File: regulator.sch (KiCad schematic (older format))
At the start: 28 parts, among them IC1 PIC12F675-I/P, Q1 PN2222A, Q2 2N2907A, Q3 BUK9511-55A (Logic Level), Q4 PN2222A, Q5 BUK9511-55A (Logic Level), U1 LM7805

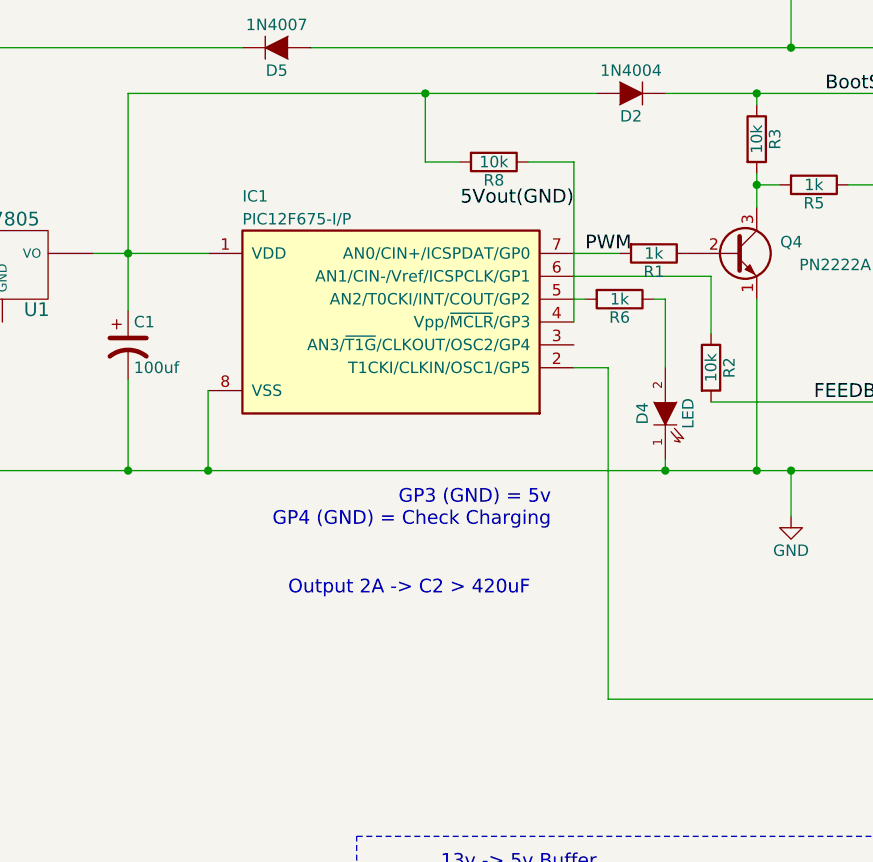
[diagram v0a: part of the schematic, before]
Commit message: Change schematic. It's not compatible with previous. Use VREF for ADC. It help under 5V output setting. ADC pin and LED pin is changed.
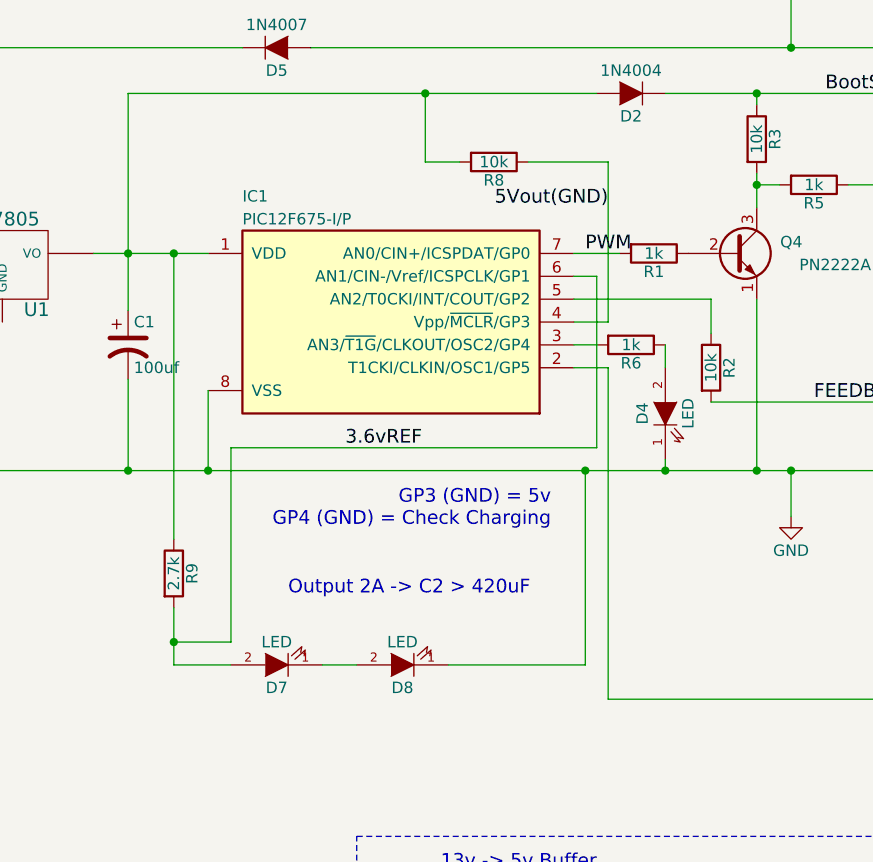
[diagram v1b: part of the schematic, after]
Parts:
- added D7, D8: LED, symbol LED
- added R9: 2.7k, symbol R
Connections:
- net GND: now also D8.1 (K)
- net at C1.1, D2.2 (A), IC1.1 (VDD)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: now also R9.1
- net at IC1.3 (AN3/~T1G~/CLKOUT/OSC2/GP4): now also R6.2
- net at IC1.5 (AN2/T0CKI/INT/COUT/GP2): now also R2.1; no longer R6.2
- net 3.6vREF: now reaches IC1.6 (AN1/CIN-/Vref/ICSPCLK/GP1)
- net 3.6vREF: now also D7.2 (A), R9.2; no longer R2.1
- new net: D7.1 (K), D8.2 (A)
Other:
- moved on the sheet: R6
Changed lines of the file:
@@
 Sheet 1 1
 Title "PWM Regulator v3"
-Date "2015-08-03"
-Rev "1.2k"
+Date "2015-08-05"
+Rev "1.3"
 Comp ""
 Comment1 ""
@@
 L R R6
 U 1 1 55680C08
-P 4050 2950
-F 0 "R6" V 4130 2950 50  0000 C CNN
-F 1 "1k" V 4050 2950 50  0000 C CNN
-F 2 "" V 3980 2950 30  0000 C CNN
-F 3 "" H 4050 2950 30  0000 C CNN
-	1    4050 2950
+P 4100 3150
+F 0 "R6" V 4180 3150 50  0000 C CNN
+F 1 "1k" V 4100 3150 50  0000 C CNN
+F 2 "" V 4030 3150 30  0000 C CNN
+F 3 "" H 4100 3150 30  0000 C CNN
+	1    4100 3150
 	0    1    1    0
 $EndComp
@@
 	0    1    1    0
 $EndComp
-Text Label 3850 2550 2    60   ~ 0
+Text Label 4000 2550 2    60   ~ 0
 5Vout(GND)
 Text Notes 3750 3950 2    60   ~ 0
@@
 Text GLabel 5050 5650 2    60   Output ~ 0
 Vto5v(+)
+Text Notes 3950 5450 2    60   ~ 0
+13v -> 5v Buffer
+$Comp
+L LED D7
+U 1 1 55C1B6BA
+P 2550 4550
+F 0 "D7" H 2550 4650 50  0000 C CNN
+F 1 "LED" H 2550 4450 50  0000 C CNN
+F 2 "" H 2550 4550 60  0000 C CNN
+F 3 "" H 2550 4550 60  0000 C CNN
+	1    2550 4550
+	-1   0    0    1
+$EndComp
+$Comp
+L LED D8
+U 1 1 55C1B8A3
+P 3100 4550
+F 0 "D8" H 3100 4650 50  0000 C CNN
+F 1 "LED" H 3100 4450 50  0000 C CNN
+F 2 "" H 3100 4550 60  0000 C CNN
+F 3 "" H 3100 4550 60  0000 C CNN
+	1    3100 4550
+	-1   0    0    1
+$EndComp
+$Comp
+L R R9
+U 1 1 55C1B943
+P 2100 4150
+F 0 "R9" V 2180 4150 50  0000 C CNN
+F 1 "2.7k" V 2100 4150 50  0000 C CNN
+F 2 "" V 2030 4150 30  0000 C CNN
+F 3 "" H 2100 4150 30  0000 C CNN
+	1    2100 4150
+	1    0    0    -1
+$EndComp
 Wire Wire Line
 	4800 3700 4800 3900
@@
 	5200 2450 5200 3000
 Wire Wire Line
-	3850 2850 4450 2850
-Wire Wire Line
-	4450 2850 4450 3100
-Wire Wire Line
 	4650 2400 4650 2550
 Wire Wire Line
@@
 	4800 1500 4800 1850
 Wire Wire Line
-	3900 2950 3850 2950
-Wire Wire Line
-	4200 2950 4250 2950
-Wire Wire Line
-	4250 2950 4250 3250
-Wire Wire Line
 	4250 3650 4250 3700
 Connection ~ 4250 3700
@@
 	1350 1500 4800 1500
 Wire Wire Line
-	3650 2350 3850 2350
-Wire Wire Line
-	3850 2350 3850 3050
+	3650 2350 4000 2350
 Wire Wire Line
 	3350 2350 3200 2350
@@
 	4650 5850 4650 5650
 Connection ~ 4650 5650
-Text Notes 3950 5450 2    60   ~ 0
-13v -> 5v Buffer
 Wire Notes Line
 	2900 5300 5600 5300
@@
 Wire Notes Line
 	2900 6750 2900 5300
+Wire Wire Line
+	3850 3050 4000 3050
+Wire Wire Line
+	4000 3050 4000 2350
+Wire Wire Line
+	4250 3250 4250 3150
+Wire Wire Line
+	3950 3150 3850 3150
+Wire Wire Line
+	4450 3100 4450 2950
+Wire Wire Line
+	4450 2950 3850 2950
+Wire Wire Line
+	2100 4300 2100 4550
+Wire Wire Line
+	2100 4550 2350 4550
+Wire Wire Line
+	3300 4550 3900 4550
+Wire Wire Line
+	3900 4550 3900 3700
+Connection ~ 3900 3700
+Wire Wire Line
+	2100 4000 2100 2750
+Connection ~ 2100 2750
+Wire Wire Line
+	2750 4550 2900 4550
+Wire Wire Line
+	3850 2850 3950 2850
+Wire Wire Line
+	3950 2850 3950 3600
+Wire Wire Line
+	3950 3600 2350 3600
+Wire Wire Line
+	2350 3600 2350 4450
+Wire Wire Line
+	2350 4450 2100 4450
+Connection ~ 2100 4450
+Text Label 2850 3600 0    60   ~ 0
+3.6vREF
 $EndSCHEMATC
